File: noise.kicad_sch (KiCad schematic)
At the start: 15 parts, among them SW1 SW_SP3T

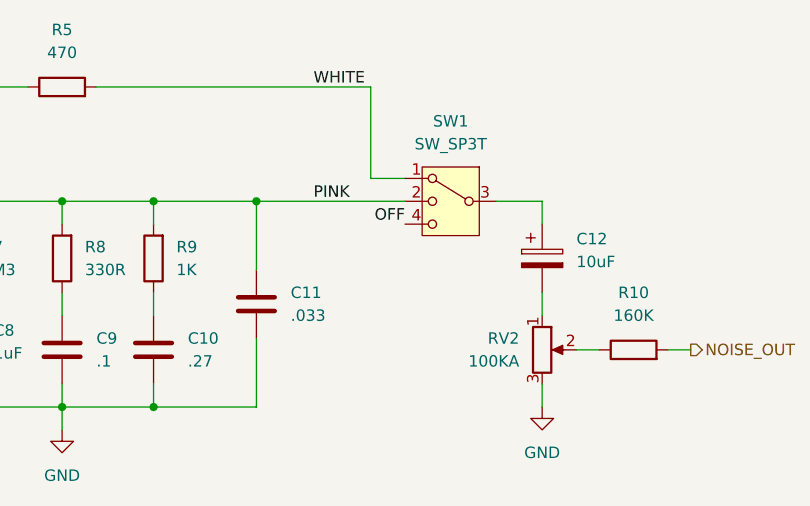
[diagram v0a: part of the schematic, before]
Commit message: Extract keyboard
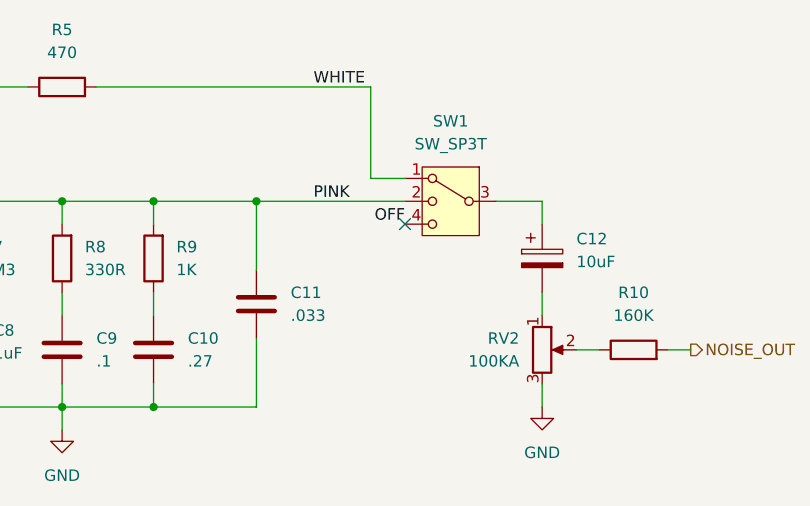
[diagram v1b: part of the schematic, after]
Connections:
- no-connect marks 0 -> 1
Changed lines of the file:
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@@
 		(color 0 0 0 0)
+	)
+	(no_connect
+		(at 181.61 90.17)
 	)
 	(wire

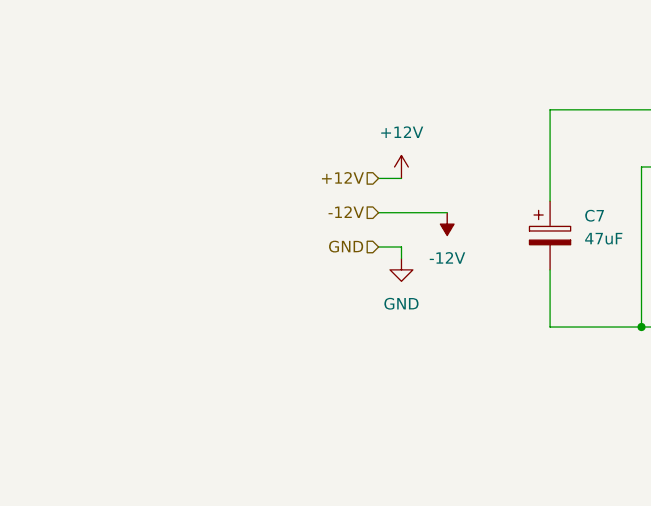
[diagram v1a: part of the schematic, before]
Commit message: Add missing values and connectors
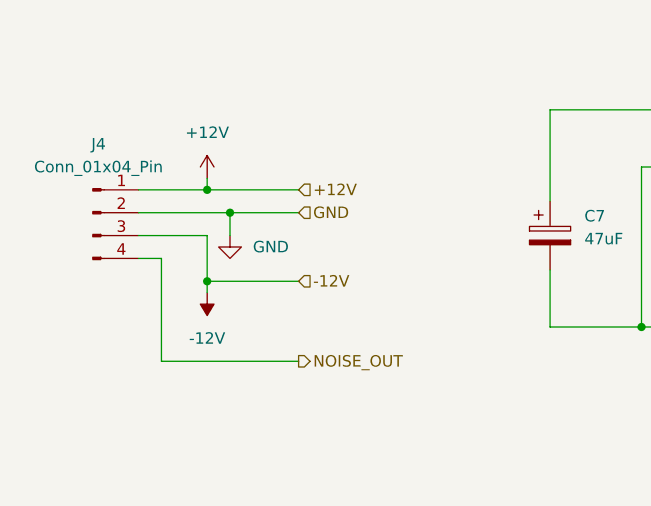
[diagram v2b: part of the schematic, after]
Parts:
- added J4: Conn_01x04_Pin, symbol Connector:Conn_01x04_Pin
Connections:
- net +12V: now also J4.1 (Pin_1)
- net -12V: now also J4.3 (Pin_3)
- net GND: now also J4.2 (Pin_2)
- net NOISE_OUT: now also J4.4 (Pin_4)

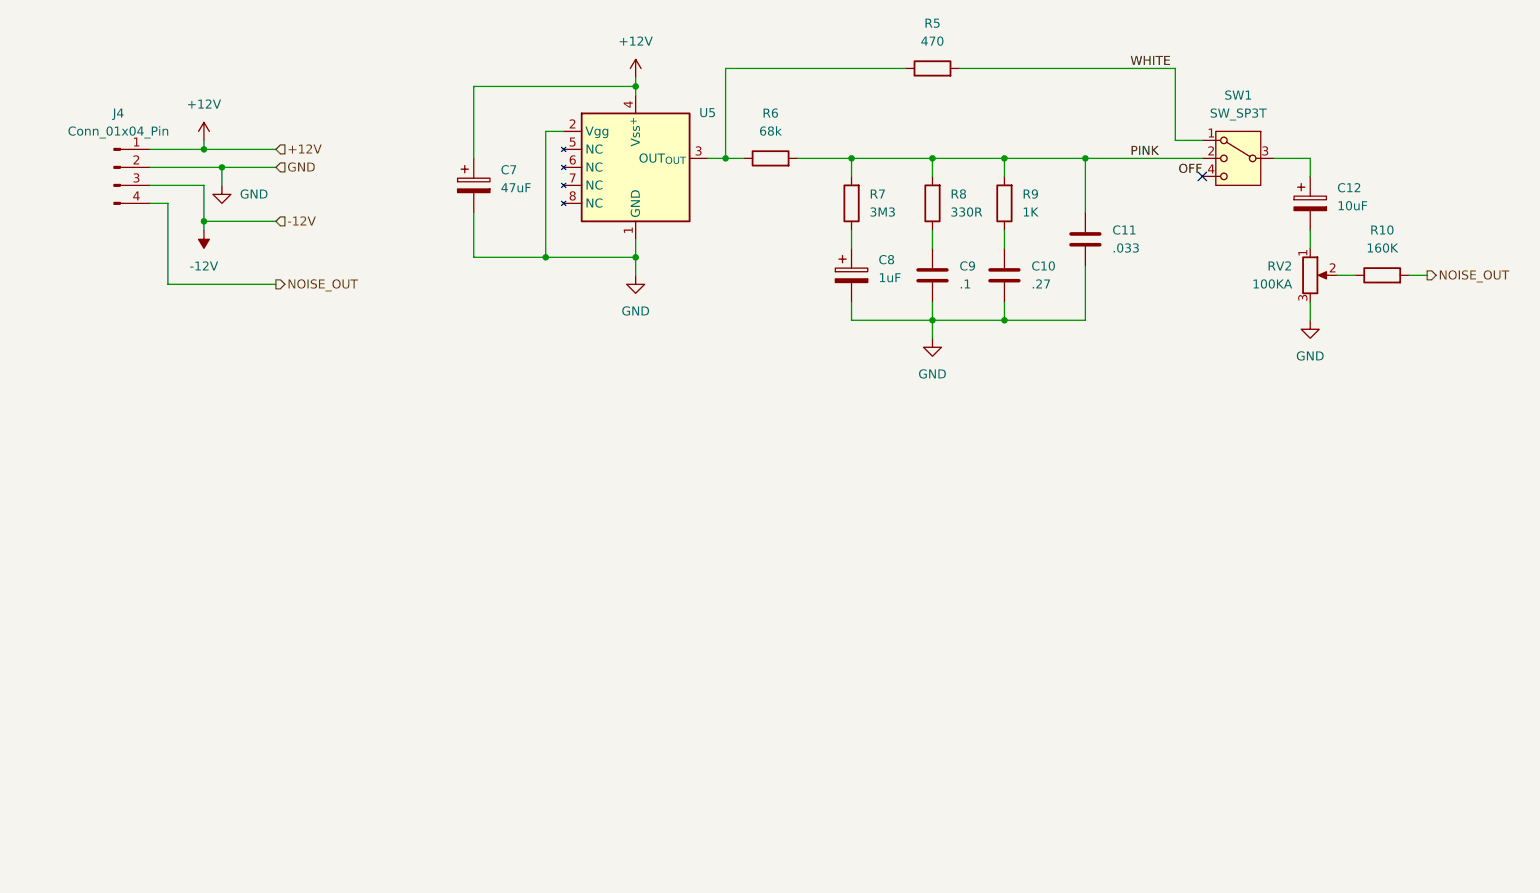
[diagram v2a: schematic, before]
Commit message: Assign footprints and start PCB
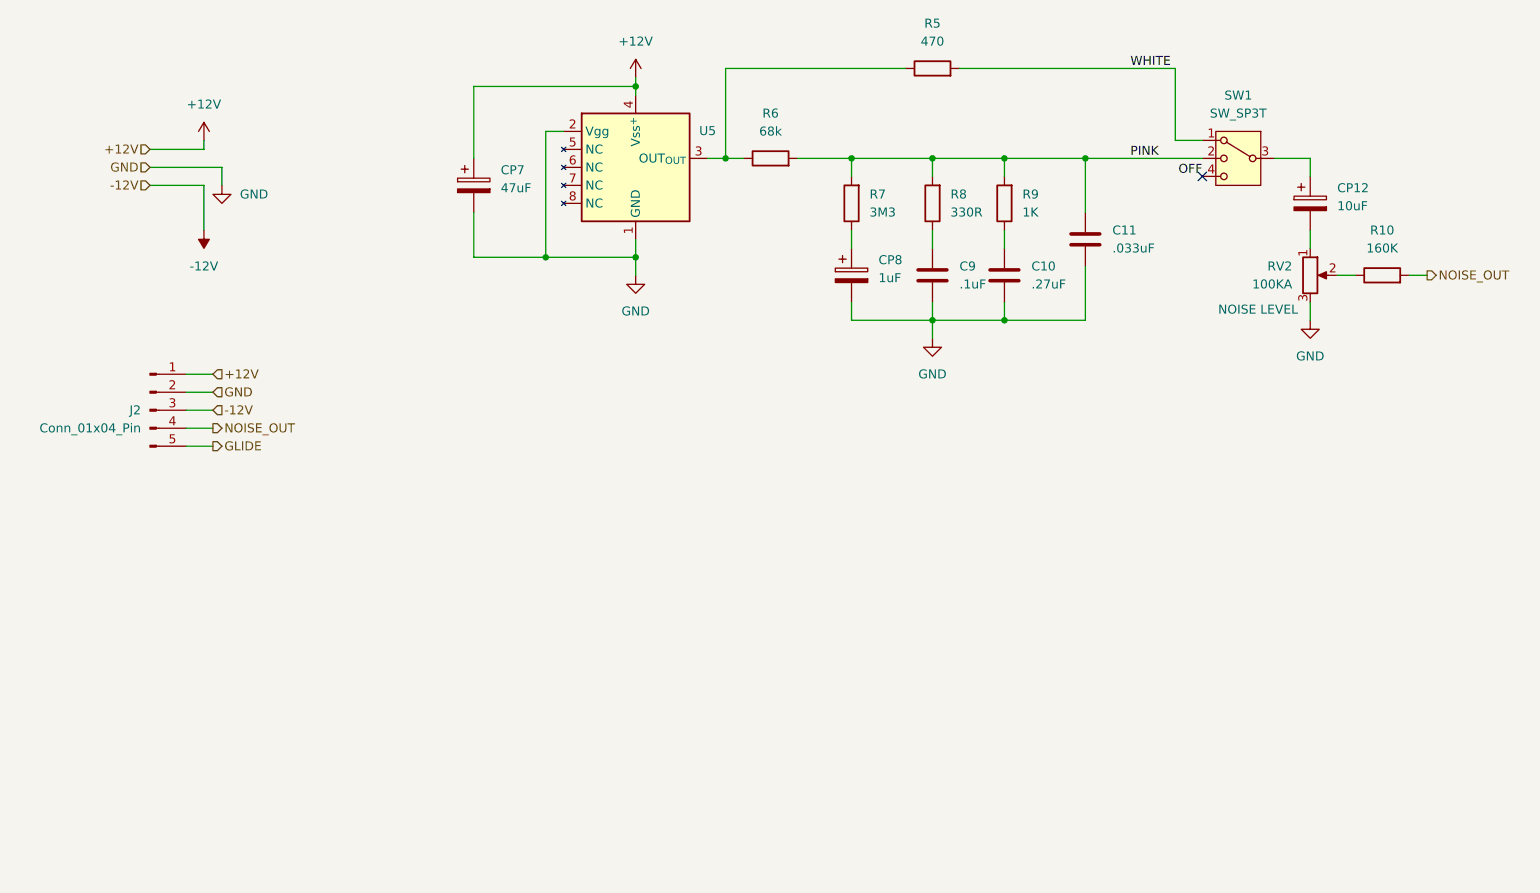
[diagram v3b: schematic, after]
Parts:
- removed J4: Conn_01x04_Pin, symbol Connector:Conn_01x04_Pin
- added J2: Conn_01x04_Pin, Connector_PinHeader_2.54mm:PinHeader_1x05_P2.54mm_Vertical, symbol Connector:Conn_01x05_Pin
- C10: value .27 -> .27uF; footprint (none) -> Capacitor_THT:C_Disc_D5.0mm_W2.5mm_P5.00mm
- C11: value .033 -> .033uF; footprint (none) -> Capacitor_THT:C_Disc_D5.0mm_W2.5mm_P5.00mm
- C9: value .1 -> .1uF; footprint (none) -> Capacitor_THT:C_Disc_D5.0mm_W2.5mm_P5.00mm
- CP12: renamed from C12; footprint (none) -> Capacitor_THT:CP_Radial_D8.0mm_P3.80mm
- CP7: renamed from C7; footprint (none) -> Capacitor_THT:CP_Radial_D8.0mm_P3.80mm
- CP8: renamed from C8; footprint (none) -> Capacitor_THT:CP_Radial_D8.0mm_P3.80mm
- R10, R5, R6, R7, R8, R9: footprint (none) -> Resistor_THT:R_Axial_DIN0204_L3.6mm_D1.6mm_P7.62mm_Horizontal
- RV2: footprint (none) -> Potentiometer_THT:Potentiometer_Omeg_PC16BU_Vertical
- SW1: footprint (none) -> Button_Switch_THT:SR2511F-0403-(L)K0A-C9-S-3_1
- U5: value ~ -> MM5837; footprint (none) -> Package_DIP:DIP-8_W7.62mm_LongPads
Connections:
- net +12V: now also J2.1 (Pin_1)
- net -12V: now also J2.3 (Pin_3)
- net GND: now also J2.2 (Pin_2)
- net NOISE_OUT: now also J2.4 (Pin_4)
- new net GLIDE: J2.5 (Pin_5)

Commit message: Added layout photos, noise & ADSR components are in position
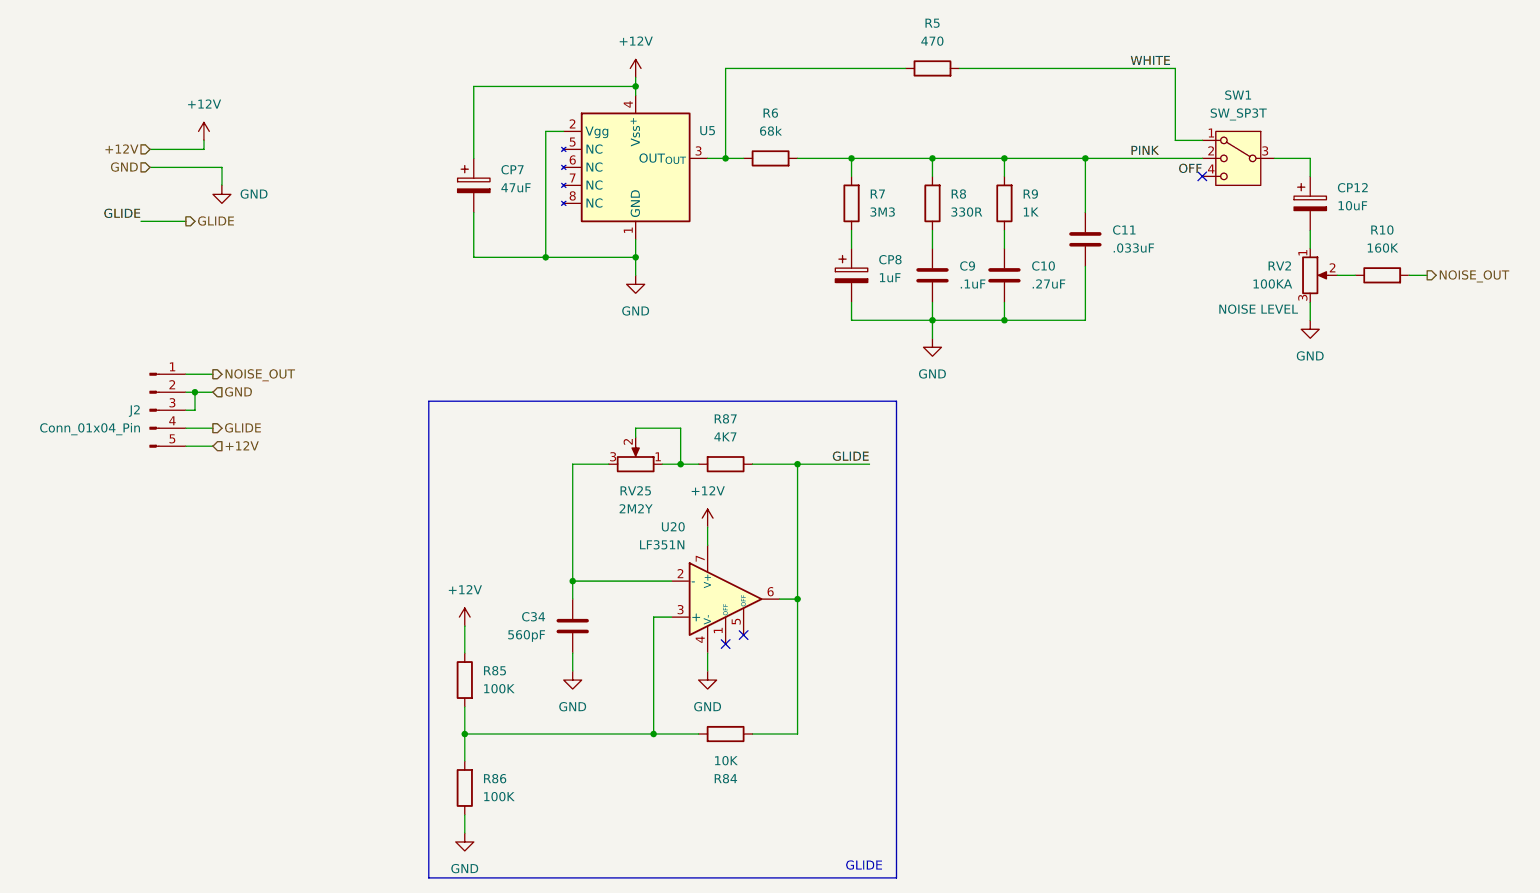
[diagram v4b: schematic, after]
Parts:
- added C34: 560pF, Capacitor_THT:C_Disc_D5.0mm_W2.5mm_P5.00mm, symbol Device:C
- added R84: 10K, Resistor_THT:R_Axial_DIN0207_L6.3mm_D2.5mm_P15.24mm_Horizontal, symbol Device:R
- added R85, R86: 100K, Resistor_THT:R_Axial_DIN0207_L6.3mm_D2.5mm_P15.24mm_Horizontal, symbol Device:R
- added R87: 4K7, Resistor_THT:R_Axial_DIN0207_L6.3mm_D2.5mm_P15.24mm_Horizontal, symbol Device:R
- added RV25: 2M2Y, Potentiometer_THT:Potentiometer_Omeg_PC16BU_Vertical, symbol Device:R_Potentiometer
- added U20: LF351N, PCM_Package_DIP_AKL:DIP-8_W7.62mm_LongPads, symbol PCM_Amplifier_Operational_AKL:LF351N
- CP12: footprint Capacitor_THT:CP_Radial_D8.0mm_P3.80mm -> Capacitor_THT:C_Disc_D5.0mm_W2.5mm_P5.00mm
- R10, R5, R6, R7, R8, R9: footprint Resistor_THT:R_Axial_DIN0204_L3.6mm_D1.6mm_P7.62mm_Horizontal -> Resistor_THT:R_Axial_DIN0207_L6.3mm_D2.5mm_P15.24mm_Horizontal
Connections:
- net -12V is gone; now on net GND: J2.3 (Pin_3)
- net +12V: now also J2.5 (Pin_5), R85.1, U20.7 (V+); no longer J2.1 (Pin_1)
- net GLIDE: now also J2.4 (Pin_4), R84.1, R87.1, U20.6; no longer J2.5 (Pin_5)
- net GND: now also C34.2, R86.1, U20.4 (V-)
- net NOISE_OUT: now also J2.1 (Pin_1); no longer J2.4 (Pin_4)
- new net: R84.2, R85.2, R86.2, U20.3 (+)
- new net: C34.1, RV25.3, U20.2 (-)
- new net: R87.2, RV25.1, RV25.2
- no-connect marks 1 -> 3
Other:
- note added: "GLIDE"

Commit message: VCO components are in position
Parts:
- C10: footprint Capacitor_THT:C_Disc_D5.0mm_W2.5mm_P5.00mm -> Capacitor_THT:C_Rect_L16.5mm_W4.7mm_P15.00mm_MKT
- C11: footprint Capacitor_THT:C_Disc_D5.0mm_W2.5mm_P5.00mm -> Capacitor_THT:C_Rect_L11.0mm_W2.8mm_P10.00mm_MKT
- CP12: footprint Capacitor_THT:C_Disc_D5.0mm_W2.5mm_P5.00mm -> Capacitor_THT:CP_Radial_D8.0mm_P5.00mm
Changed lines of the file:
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@@
 			)
 		)
-		(property "Footprint" "Capacitor_THT:C_Disc_D5.0mm_W2.5mm_P5.00mm"
+		(property "Footprint" "Capacitor_THT:C_Rect_L11.0mm_W2.8mm_P10.00mm_MKT"
 			(at 166.0652 102.87 0)
 			(effects
@@
 			)
 		)
-		(property "Footprint" "Capacitor_THT:C_Disc_D5.0mm_W2.5mm_P5.00mm"
+		(property "Footprint" "Capacitor_THT:CP_Radial_D8.0mm_P5.00mm"
 			(at 197.8152 97.79 0)
 			(effects
@@
 			)
 		)
-		(property "Footprint" "Capacitor_THT:C_Disc_D5.0mm_W2.5mm_P5.00mm"
+		(property "Footprint" "Capacitor_THT:C_Rect_L16.5mm_W4.7mm_P15.00mm_MKT"
 			(at 154.6352 107.95 0)
 			(effects

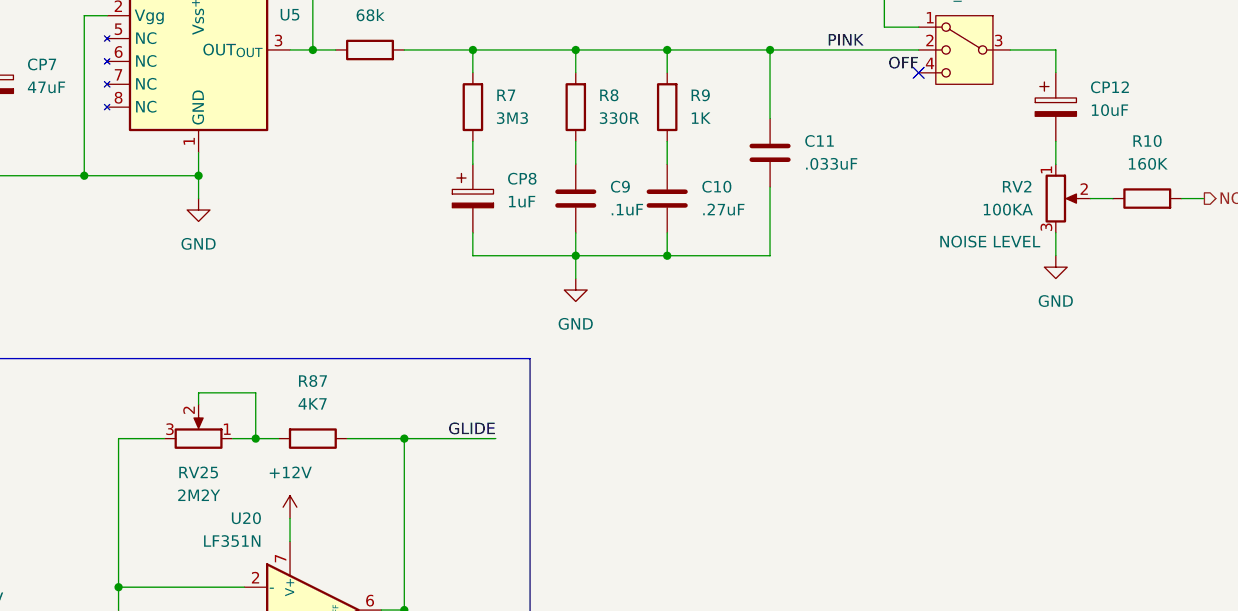
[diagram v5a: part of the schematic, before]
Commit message: Fix PCB sizes, adjust layout to new size
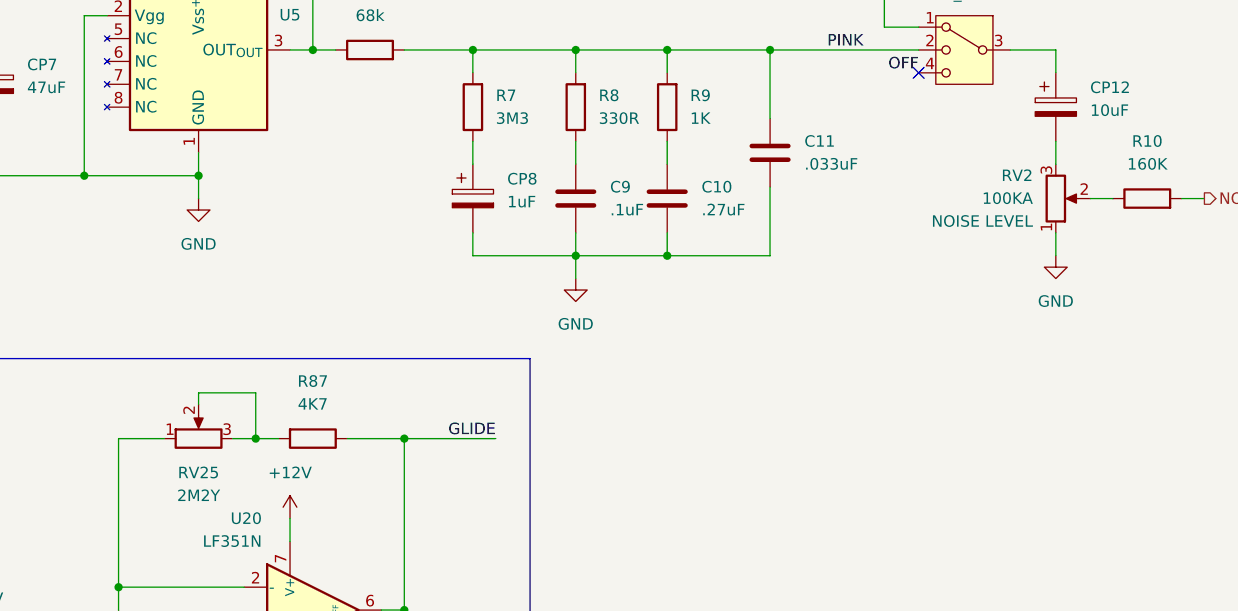
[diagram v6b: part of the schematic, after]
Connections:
- net GND: now also RV2.1; no longer RV2.3
- net at C34.1, U20.2 (-): now also RV25.1; no longer RV25.3
- net at CP12.2: now also RV2.3; no longer RV2.1
- net at R87.2, RV25.2: now also RV25.3; no longer RV25.1
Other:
- moved on the sheet: RV25
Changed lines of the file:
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@@
 	(symbol
 		(lib_id "Device:R_Potentiometer")
-		(at 101.6 130.81 270)
-		(mirror x)
-		(unit 1)
-		(exclude_from_sim no)
-		(in_bom yes)
-		(on_board yes)
-		(dnp no)
-		(fields_autoplaced yes)
+		(at 101.6 130.81 90)
+		(unit 1)
+		(exclude_from_sim no)
+		(in_bom yes)
+		(on_board yes)
+		(dnp no)
 		(property "Reference" "RV25"
 			(at 101.6 134.62 90)
@@
 		(lib_id "Device:R_Potentiometer")
 		(at 196.85 104.14 0)
-		(unit 1)
-		(exclude_from_sim no)
-		(in_bom yes)
-		(on_board yes)
-		(dnp no)
+		(mirror x)
+		(unit 1)
+		(exclude_from_sim no)
+		(in_bom yes)
+		(on_board yes)
+		(dnp no)
+		(fields_autoplaced yes)
 		(property "Reference" "RV2"
-			(at 194.31 102.8699 0)
+			(at 194.31 101.5999 0)
 			(effects
 				(font
@@
 		)
 		(property "Value" "100KA"
-			(at 194.31 105.4099 0)
+			(at 194.31 104.1399 0)
 			(effects
 				(font
@@
 		)
 		(property "Description" "NOISE LEVEL"
-			(at 189.484 108.966 0)
-			(effects
-				(font
-					(size 1.27 1.27)
-				)
-			)
-		)
+			(at 194.31 106.6799 0)
+			(effects
+				(font
+					(size 1.27 1.27)
+				)
+				(justify right)
+			)
+		)

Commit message: Routing
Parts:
- C9: footprint Capacitor_THT:C_Disc_D5.0mm_W2.5mm_P5.00mm -> Capacitor_THT:C_Rect_L11.0mm_W2.8mm_P10.00mm_MKT
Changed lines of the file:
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@@
 			)
 		)
-		(property "Footprint" "Capacitor_THT:C_Disc_D5.0mm_W2.5mm_P5.00mm"
+		(property "Footprint" "Capacitor_THT:C_Rect_L11.0mm_W2.8mm_P10.00mm_MKT"
 			(at 144.4752 107.95 0)
 			(effects
